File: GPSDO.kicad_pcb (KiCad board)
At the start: 2 copper layers, 86 parts, among them J1 Conn_Coaxial, J10 PROG, J2 GPS_CONN, J3 Conn_Coaxial, J4 Conn_Coaxial, J5 Conn_Coaxial, J6 Conn_Coaxial, J7 DISP_MODULE, J8 Barrel_Jack, SW1 RESET_BTN, U1 REF3450, U10 MC7805BDTRKG, U11 74AUC1G74, U12 74AUC2G04, U13 74AUC2G04, U14 DS34C87T, U2 74LVC1G125SE-7, U3 AD5680, U4 NB3N551MN, U5 LTC2050IS8, U6 AVR32DB28x-xSO, U7 74LVC1G125SE-7, U8 74HC390, U9 L7805CV, X1 OCXO-14

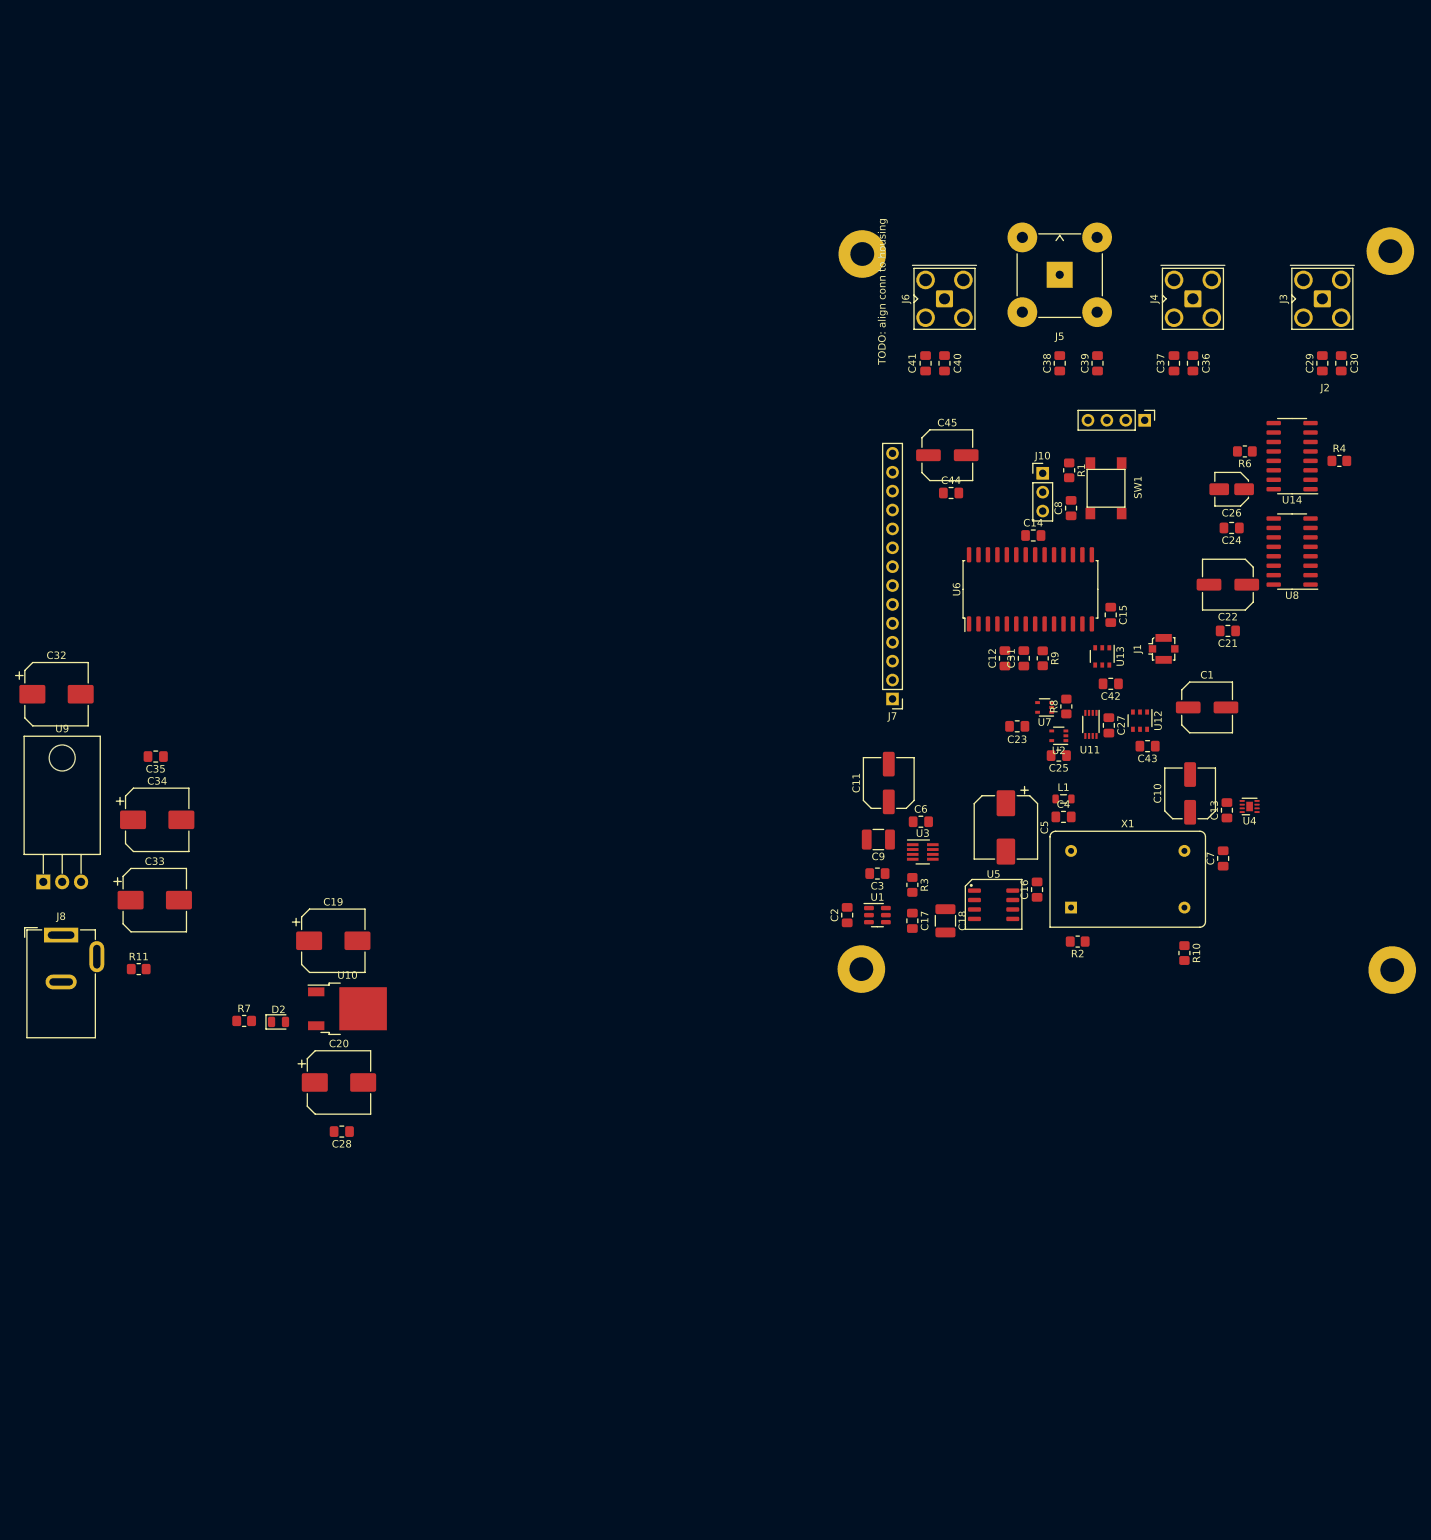
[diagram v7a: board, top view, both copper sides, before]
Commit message: finalised schematic
no more big changes
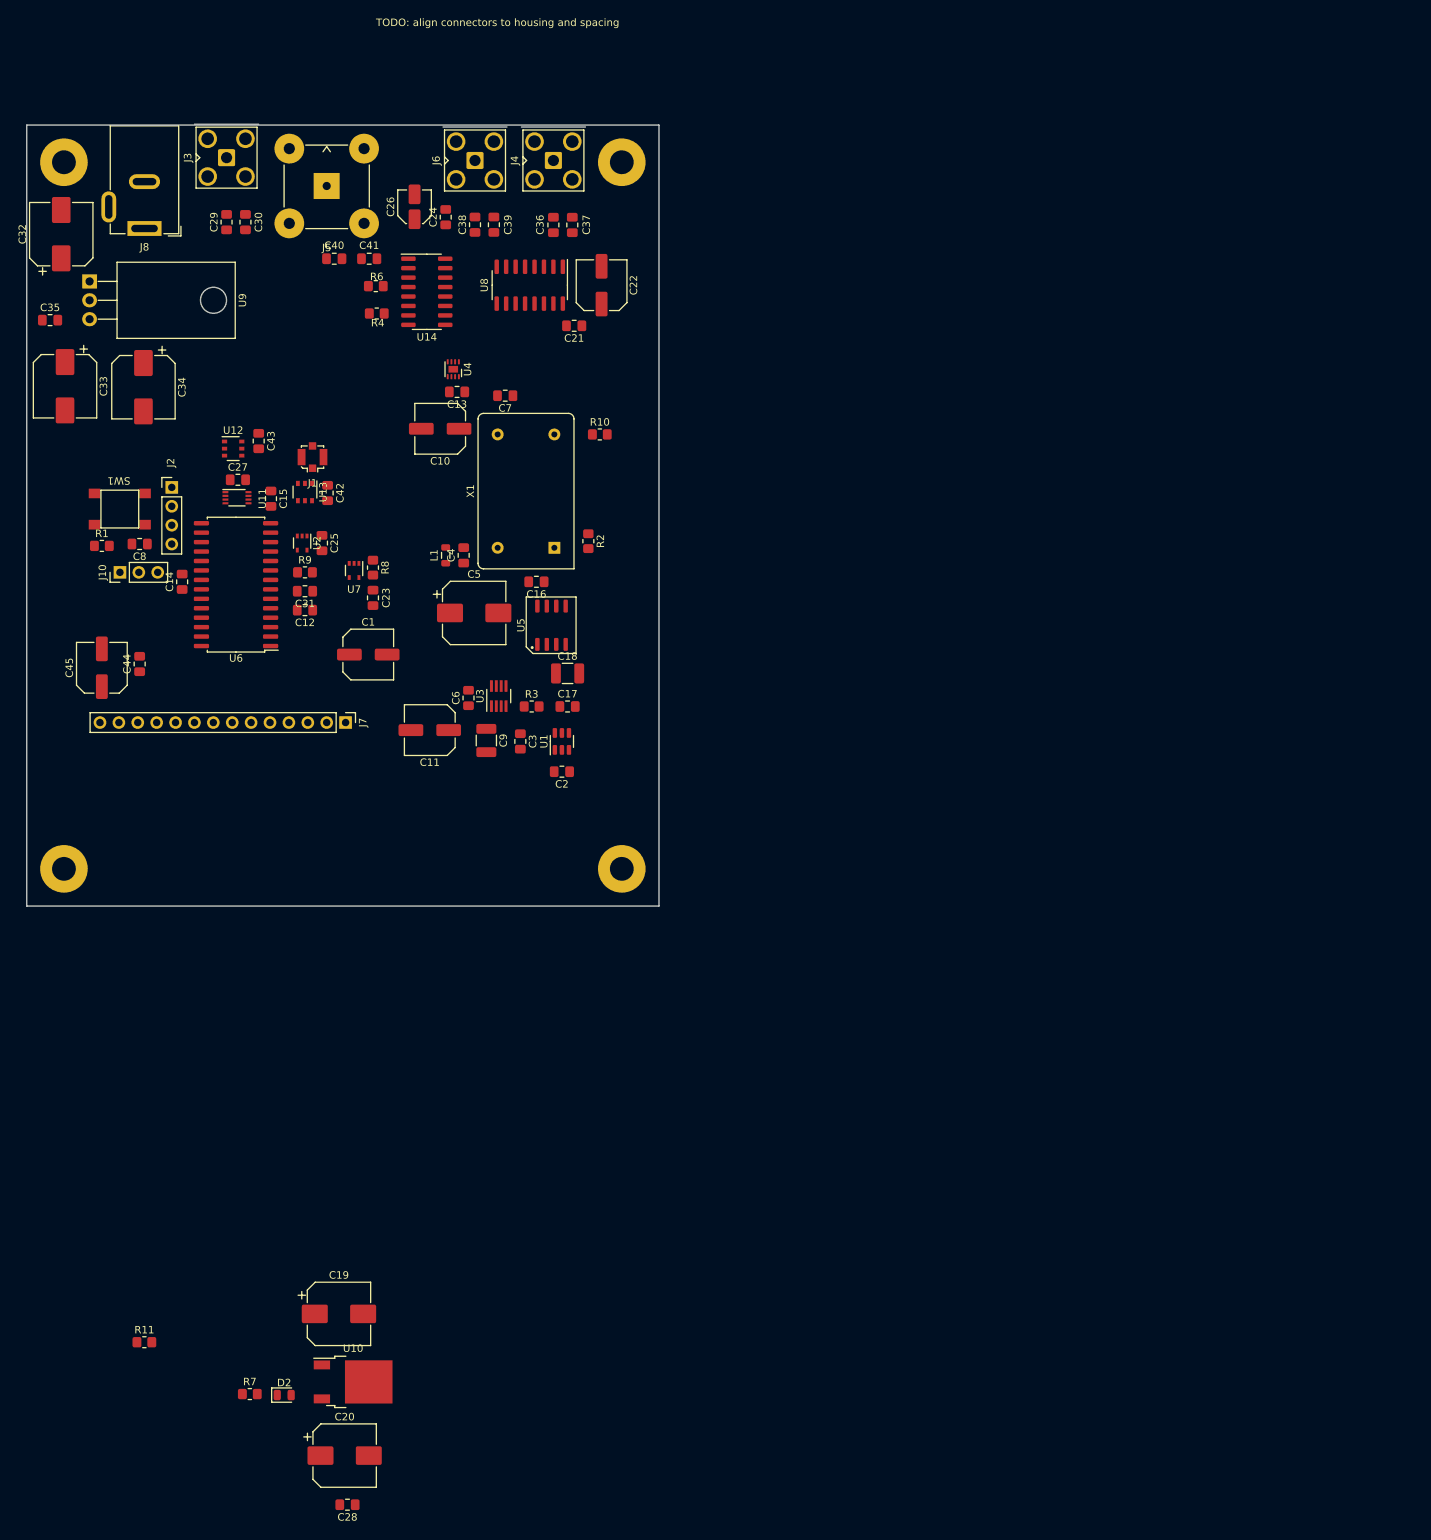
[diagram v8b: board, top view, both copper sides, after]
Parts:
- X1: value OCXO-14 -> OC5SC25
- moved C30 148.5 mm to (49.4, 33.1)
- moved C29 148.5 mm to (46.9, 33.1)
- moved J3 148.5 mm to (46.9, 24.4)
- moved SW1 132.6 mm to (32.5, 71.6), turned to 180 degrees
- moved R4 131.7 mm to (66.9, 41.7), turned to 180 degrees
- moved J2 131.1 mm to (39.5, 68.7), turned to 0 degrees
- moved R1 130.4 mm to (30.1, 76.6), turned to 0 degrees
- moved U12 127.3 mm to (47.8, 63.5), turned to 0 degrees
- moved C43 126.4 mm to (51.2, 62.5), turned to -90 degrees
- moved C8 125.3 mm to (35.2, 76.3), turned to 180 degrees
- moved J10 124.8 mm to (32.5, 80.1), turned to 90 degrees
- moved U4 122.1 mm to (77.3, 52.8), turned to -90 degrees
- moved C27 121.7 mm to (48.4, 67.7), turned to 0 degrees
- moved U11 118.8 mm to (48.3, 70.1), turned to 0 degrees
- moved U14 118.4 mm to (73.8, 42.4), turned to 0 degrees
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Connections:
- C29 pad 1: Net-(C29-Pad1) -> Net-(U14-Pad5)
- C30 pad 1: Net-(C30-Pad1) -> Net-(U14-Pad6)
- C36 pad 1: Net-(C36-Pad1) -> Net-(U14-Pad11)
- C37 pad 1: Net-(C37-Pad1) -> Net-(U14-Pad10)
- C38 pad 1: Net-(C38-Pad1) -> Net-(U14-Pad13)
- C39 pad 1: Net-(C39-Pad1) -> Net-(U14-Pad14)
- C40 pad 1: Net-(C40-Pad1) -> Net-(U14-Pad3)
- C41 pad 1: Net-(C41-Pad1) -> Net-(U14-Pad2)
- J5 pad 1: Net-(C38-Pad2) -> Net-(C40-Pad2)
- J5 pad 2: Net-(C39-Pad2) -> Net-(C41-Pad2)
- J6 pad 1: Net-(C40-Pad2) -> Net-(C38-Pad2)
- J6 pad 2: Net-(C41-Pad2) -> Net-(C39-Pad2)
- J7 pad 2: /LCD_MISO -> /TOUCH_MISO
- J7 pad 8: /DAC_SCK -> /LCD_SCK
- J7 pad 9: /DAC_MOSI -> /LCD_MOSI
- U14 pad 1: /MAIN_CLK_2 -> /MAIN_CLK_3
- U14 pad 10: Net-(C39-Pad1) -> Net-(U14-Pad10)
- U14 pad 11: Net-(C38-Pad1) -> Net-(U14-Pad11)
- U14 pad 13: Net-(C40-Pad1) -> Net-(U14-Pad13)
- U14 pad 14: Net-(C41-Pad1) -> Net-(U14-Pad14)
- U14 pad 15: /10Mc_CLK -> /5Mc_CLK
- U14 pad 2: Net-(C30-Pad1) -> Net-(U14-Pad2)
- U14 pad 3: Net-(C29-Pad1) -> Net-(U14-Pad3)
- U14 pad 5: Net-(C36-Pad1) -> Net-(U14-Pad5)
- U14 pad 6: Net-(C37-Pad1) -> Net-(U14-Pad6)
- U14 pad 9: /10Mc_CLK -> /MAIN_CLK_2
- U6 pad 10: /~{GAL} -> unconnected-(U6-Pad10)
- U6 pad 11: /~{GAU} -> /TOUCH_IRQ
- U6 pad 12: /~{GBL} -> /FF_SET
- U6 pad 13: /~{GBU} -> /FF_RESET
- U6 pad 2: /~{LCD_SS} -> /LCD_MOSI
- U6 pad 27: /LCD_MISO -> /TOUCH_MISO
- U6 pad 3: /FF_RESET -> /LCD_MISO
- U6 pad 4: /FF_SET -> /LCD_SCK
- U6 pad 5: /TOUCH_IRQ -> /~{LCD_SS}
- U8 pad 13: /10Mc_CLK -> /5Mc_CLK
- U8 pad 14: /DIV_RESET -> GND
- U8 pad 15: /MAIN_CLK_3 -> /MAIN_CLK_1
- U8 pad 2: /DIV_RESET -> GND
- U8 pad 4: /MAIN_CLK_3 -> /MAIN_CLK_1
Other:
- board outline added: 85 x 105 mm
- board text added: "TODO: align connectors to housing and spacing"
- board text removed: "TODO: align conn to housing"
